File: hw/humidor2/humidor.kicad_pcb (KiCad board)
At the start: 2 copper layers, 61 x 53 mm, 24 parts, among them J1 PWR IN, J2 PWR IN/EXTSENS/IND, J3 IN_SENSOR, J4 Conn_01x12, J5 HEAT/FAN/HS, Q1 2N7002, Q2 IRFD9120, Q3 IRL540, SW1 SW_Push

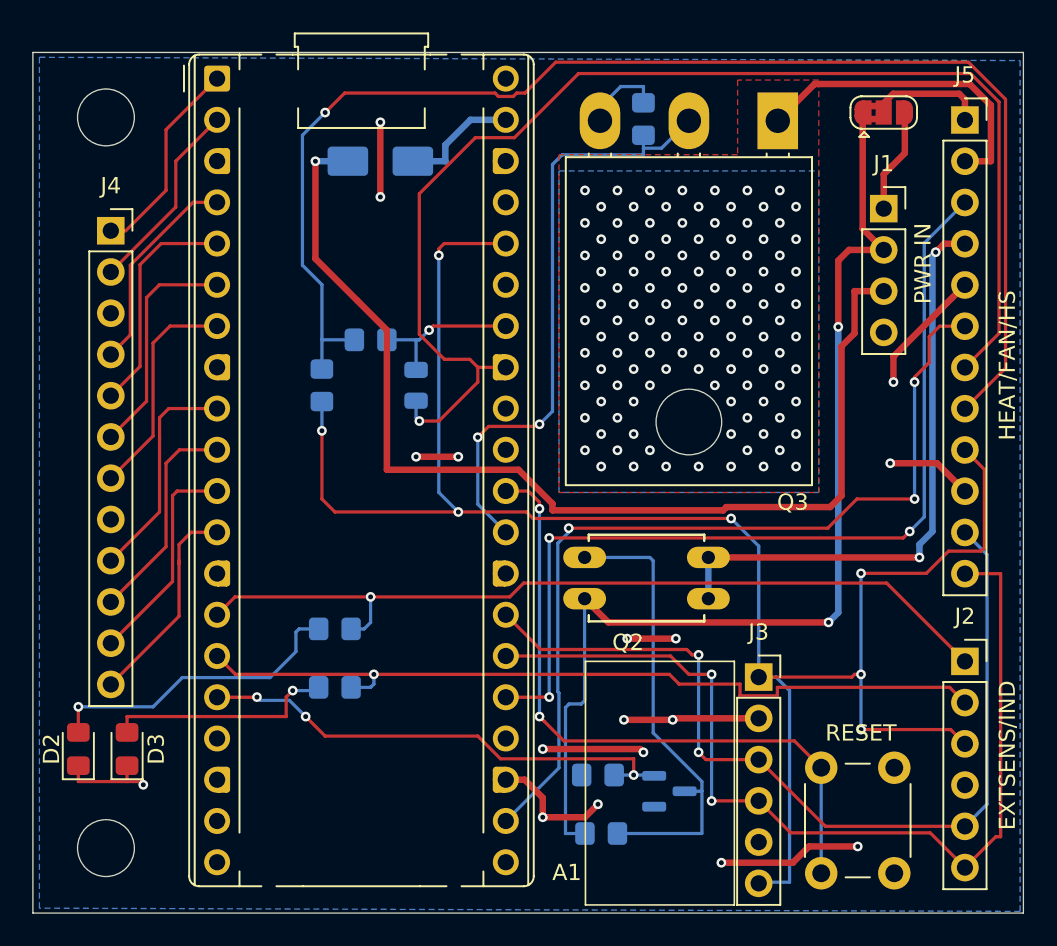
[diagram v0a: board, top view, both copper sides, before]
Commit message: functioning version on breadboard, ready for further HA integration
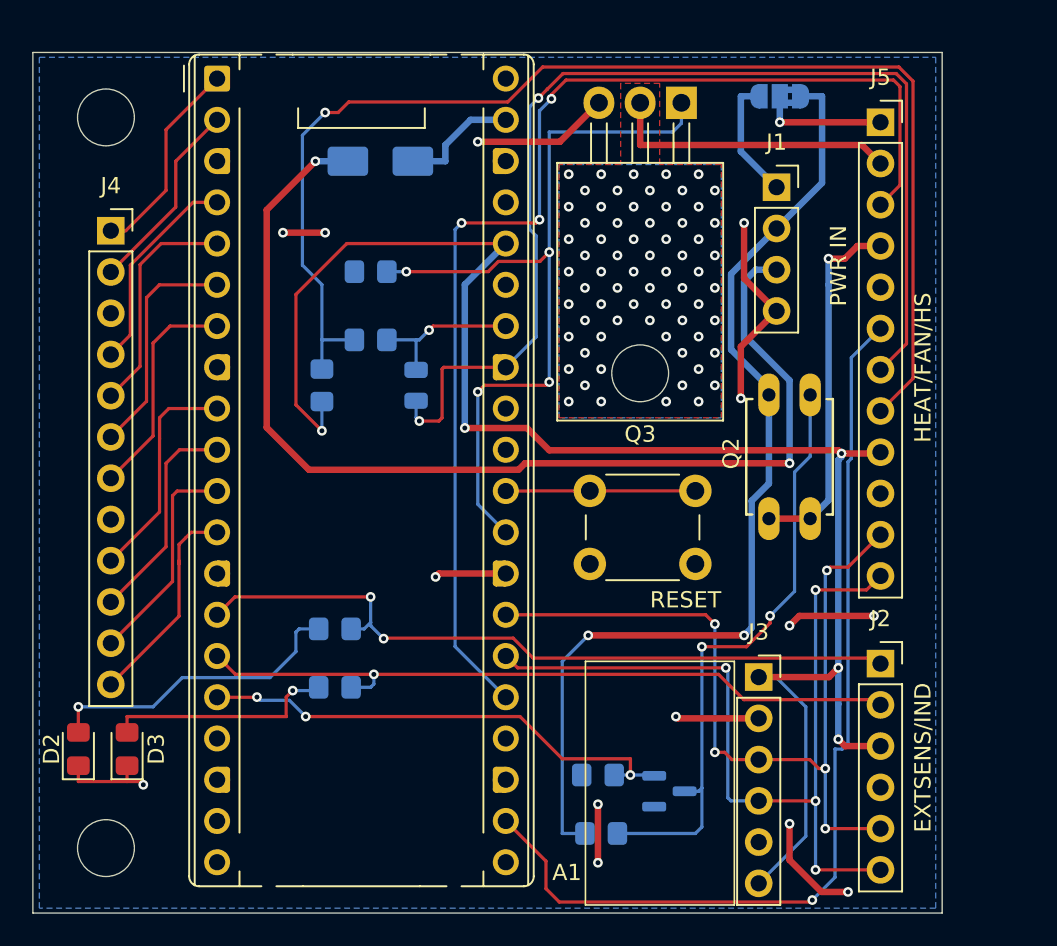
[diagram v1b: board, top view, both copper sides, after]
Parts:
- JP2: moved to B.Cu
- Q3: value IRL540 -> IRF540N; footprint Package_TO_SOT_THT:TO-218-3_Horizontal_TabDown -> Package_TO_SOT_THT:TO-220-3_Horizontal_TabDown
- moved R8 19.3 mm to (99.8, 63.0), turned to 180 degrees
- moved SW1 17.5 mm to (119.8, 81.0), turned to 180 degrees
- moved Q2 11.6 mm to (125.6, 74.4), turned to 90 degrees
- moved J1 6.73 mm to (124.8, 57.8)
- moved JP2 6.48 mm to (125.0, 52.2), turned to 180 degrees
- moved Q3 6.04 mm to (118.9, 52.6)
- moved J2 5.20 mm to (131.2, 87.1)
- moved J5 5.20 mm to (131.2, 53.8)
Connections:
- Q3 pad 1: /HEAT_SW -> /HEAT_PWM
- Q3 pad 2: /HEAT_PWM -> /HEAT_SW
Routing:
- net Net-(A1-RUN): track 40.7 -> 11.7 mm, vias 2 -> 0
- net /TACH: track 56.5 -> 73.3 mm
- net /FAN_PWR: track 36.8 -> 22.5 mm, vias 2 -> 1
- net /HEAT_PWM: track 37.6 -> 49.5 mm, vias 2 -> 4
- net +3.3V: track 116.6 -> 105.1 mm, vias 7 -> 5
- net GND: track 66.1 -> 54.9 mm, vias 17 -> 14
- net /AGND: track 78.4 -> 69.4 mm, vias 1 -> 2
- net Net-(Q1-D): track 28.6 -> 37.5 mm, vias 0 -> 2
- net /SDA0: track 59.6 -> 53.0 mm, vias 2 -> 4
- net /HEAT_ON: track 51.8 -> 45.4 mm, vias 1 -> 2
- net /FAN_ON: track 50.5 -> 44.2 mm
- net /T_HEATSINK: track 83.3 -> 77.7 mm
- net /SCL0: track 56.4 -> 51.8 mm, vias 2 -> 5
- net /FAN_PWM: track 54.6 -> 59.2 mm, vias 3 -> 1
- net +12V: track 66.8 -> 62.3 mm
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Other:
- board size 61 x 53 mm -> 56 x 53 mm
